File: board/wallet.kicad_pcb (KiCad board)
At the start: 4 copper layers, 48 x 85 mm, 108 parts, among them J1 TYPE-C-31-M-12, U1 BQ25185DLHR, U11 E73-2G4M08S1C, U12 ME6211C28M5G-N, U13 TPS60230RGTR, U14 TLV70313DBVR, U15 MAX17048G+T10, U2 TPS63802DLAR, U4 STM32U585VIT6Q, U5 SE050E2HQ1/Z01Z3Z, U6 TS3USB221ARSER, U7 SN74LVC1G02DBVR(UMW), U8 TPS22917DBVR, U9 TXU0202DCUR

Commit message: TP_NRST next to the MCU's NRST pin
The NRST test pad sat with the other programming pads on the west edge while
NRST is pin 14 on the MCU's east side, behind hand-routed copper: the autorouter
took 29.5 mm down the west edge for it. Now on the front at (33.6, 26.8), beside
NRST's 100 nF cap: 4.7 mm of copper, one via. Same move in the radio-gate
candidate. Unconnected 57 -> 56 on the main board.

Co-Authored-By: Claude Opus 5.5 <noreply@anthropic.com>
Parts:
- moved TP_NRST 29.6 mm to (33.6, 26.8)
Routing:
- net NRST: track 2.34 -> 4.73 mm, vias 0 -> 1
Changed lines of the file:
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@@
 	(footprint "TestPoint:TestPoint_Pad_D1.0mm"
 		(layer "F.Cu")
-		(at 4 25.56)
+		(at 33.6 26.8)
 		(descr "SMD pad as test Point, diameter 1.0mm")
 		(tags "test point SMD pad")
@@
 	)
 	(segment
+		(start 33.425 26.8)
+		(end 32.35 27.875)
+		(width 0.15)
+		(layer "F.Cu")
+		(net "NRST")
+	)
+	(segment
+		(start 33.6 26.8)
+		(end 33.425 26.8)
+		(width 0.15)
+		(layer "F.Cu")
+		(net "NRST")
+	)
+	(via
+		(at 32.35 27.875)
+		(size 0.45)
+		(drill 0.25)
+		(layers "F.Cu" "B.Cu")
+		(net "NRST")
+	)
+	(segment
 		(start 31.89 28.5)
 		(end 31.98 28.41)
 		(width 0.15)
+		(layer "B.Cu")
+		(net "NRST")
+	)
+	(segment
+		(start 32.35 27.875)
+		(end 32.35 28.04)
+		(width 0.15)
+		(layer "B.Cu")
+		(net "NRST")
+	)
+	(segment
+		(start 32.35 28.04)
+		(end 31.98 28.41)
+		(width 0.15)

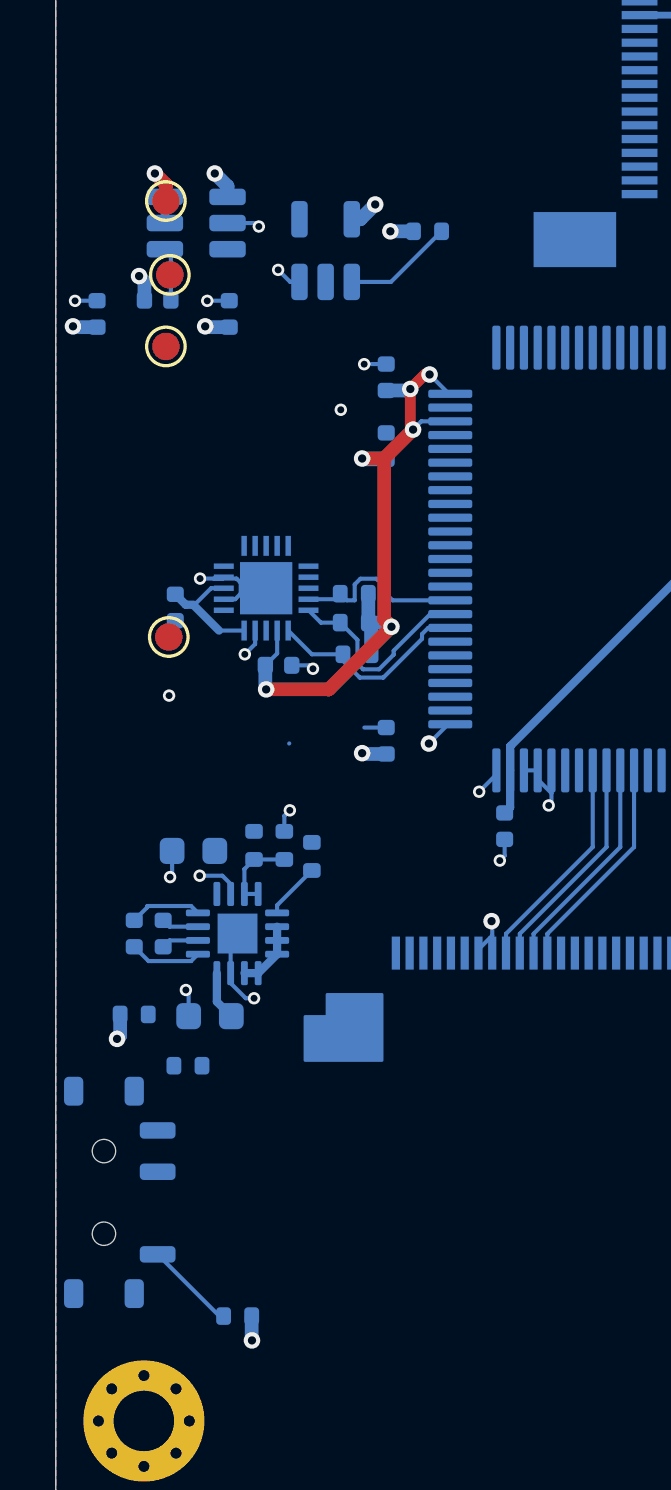
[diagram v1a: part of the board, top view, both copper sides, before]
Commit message: Radio gate beside the airgap switch (merged from the experiment)
The NOR and the load switch with their parts move from the north-west corner
to beside the airgap switch: AIRGAP and RADIO_3V3, which ran 30-40 mm down the
west side, are now a few millimetres. Gauge (full autoroute on a copy, same
settings): 10 % less copper to route (1260 vs 1395 mm), 5 fewer signal vias.
Only the radio gate's parts and my copper at them changed; the owner's copper
is untouched. Open: one 2.7 mm 3.3 V link (CT cap to the airgap pull-up) for a
hand trace, no via fits there. UV art rebuilt.

Co-Authored-By: Claude Opus 5.5 <noreply@anthropic.com>
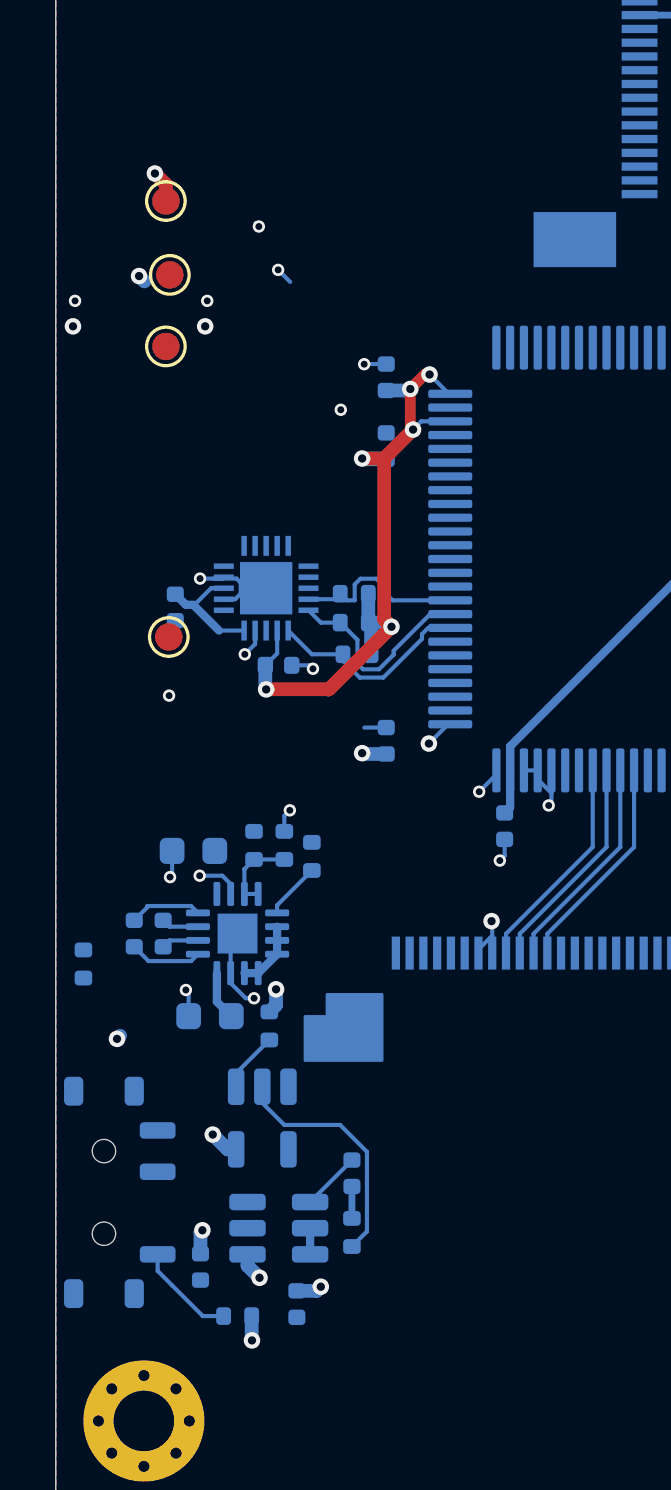
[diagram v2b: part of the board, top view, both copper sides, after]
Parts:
- moved C_RIN 36.7 mm to (8.75, 55.1), turned to -90 degrees
- moved U8 36.6 mm to (8.10, 52.3), turned to 0 degrees
- moved C_NOR 34.6 mm to (5.25, 53.7), turned to -90 degrees
- moved C_RCT 32.5 mm to (10.8, 50.3), turned to 90 degrees
- moved U7 31.6 mm to (7.50, 48.3), turned to -90 degrees
- moved R_ROFF 29.4 mm to (7.75, 45.0), turned to 90 degrees
- moved R_AIRPU 11.2 mm to (10.8, 52.5), turned to 90 degrees
- moved R_AIRS 5.30 mm to (1.00, 42.7), turned to 90 degrees
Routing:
- net AIRGAP: track 0.00 -> 8.79 mm
- net GND: track 81.9 -> 79.0 mm
- net RADIO_OFF: track 4.02 -> 2.20 mm
- net V3V3: track 112.7 -> 112.6 mm, vias 45 -> 47

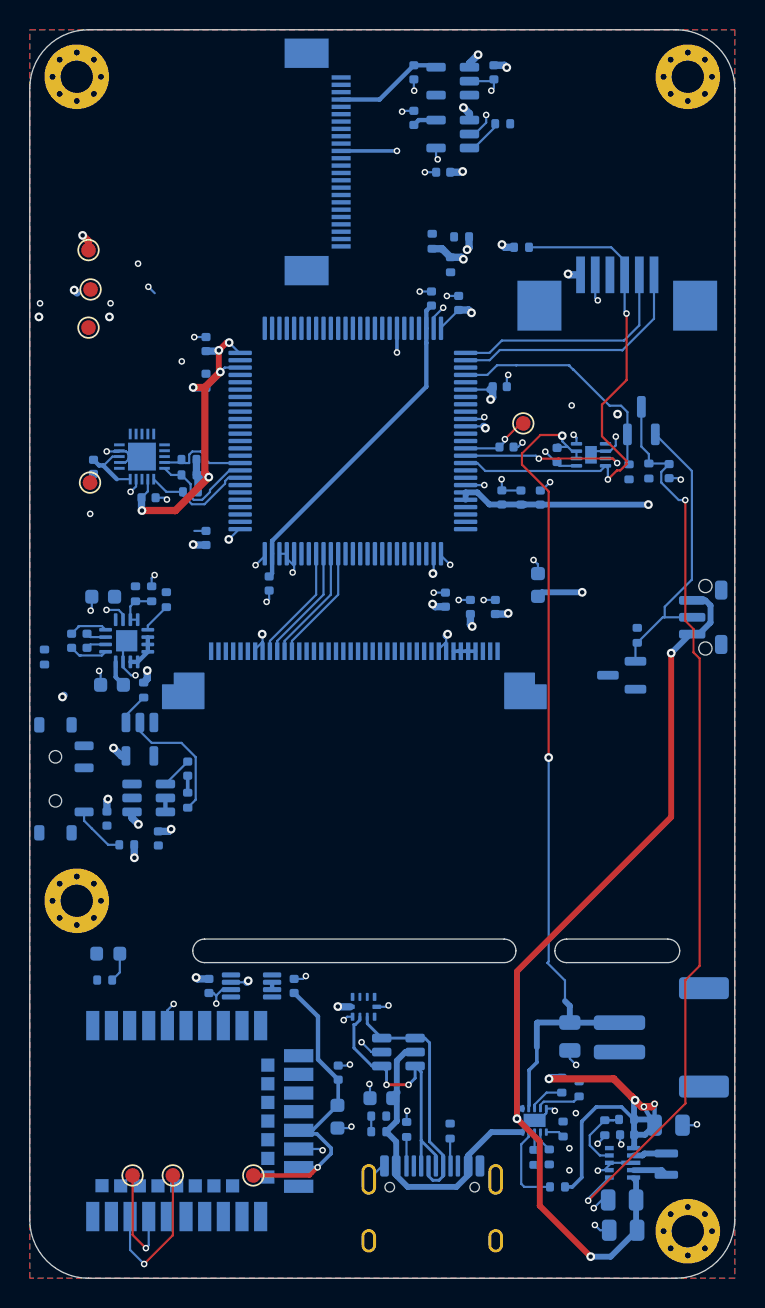
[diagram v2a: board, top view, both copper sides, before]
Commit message: Owner: north camera pins, radio UART, display control, button and 3.3 V cleanup
Hand-routed the camera bus's north-side pins (VSYNC, XCLK, D4, D6, D7, RST,
SDA, EN), the radio UART from the module to the TXU0202, TFT_TE/RST, BTN/BTN_N,
CTP_RST, I2C_SCL, AIRGAP, RADIO_3V3. Button transistor and resistor moved up by
the MCU, the AIRGAP_SENSE resistor inline by the MCU, the radio LED parts
shifted. 3.3 V cleanup: three stale plane vias (left where the radio gate's
parts used to be) and stubs removed; thin 0.15 mm 3.3 V links between a plane
via and its pad redone at 0.4 mm.

Co-Authored-By: Claude Opus 5.5 <noreply@anthropic.com>
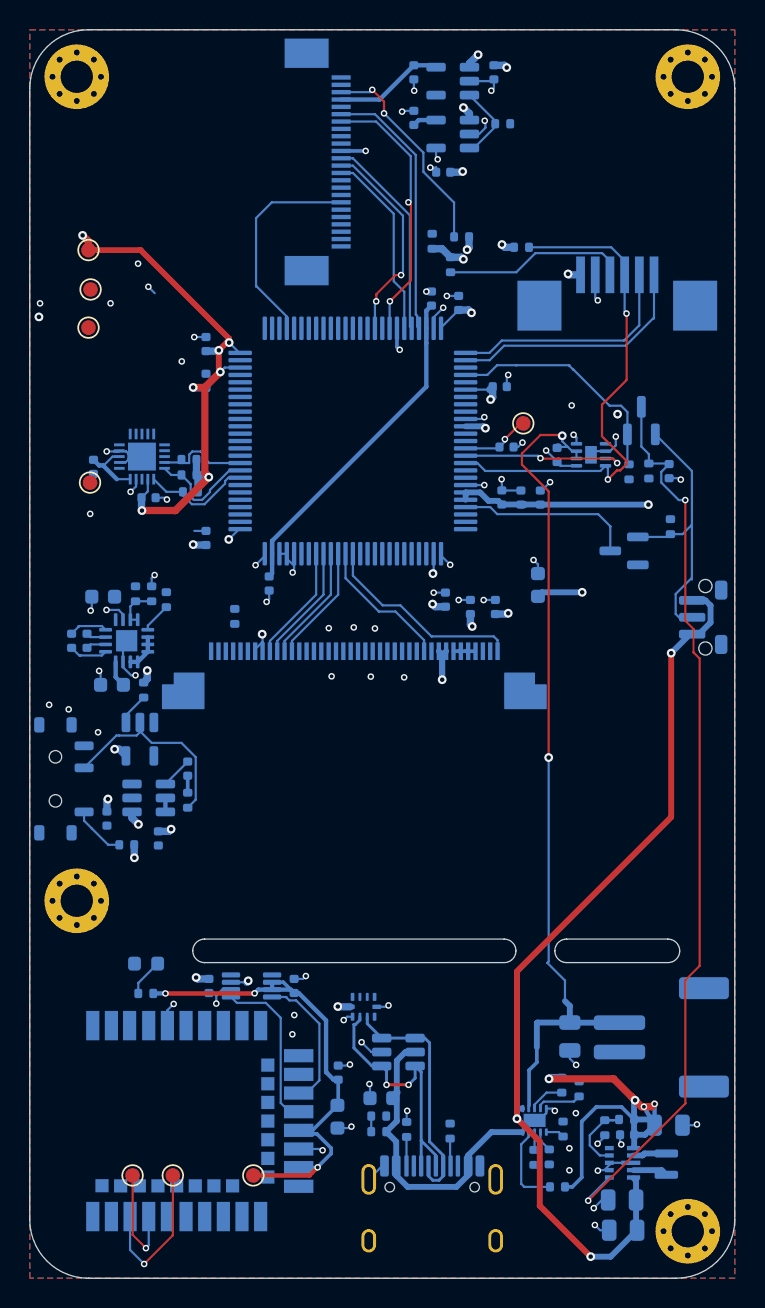
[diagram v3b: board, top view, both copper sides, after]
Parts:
- moved R_AIRS 13.2 mm to (14.0, 39.9)
- moved Q_BTN 8.47 mm to (40.5, 35.5)
- moved R_BTN 7.74 mm to (43.6, 33.8)
- moved R_RLED 2.94 mm to (7.90, 65.6), turned to 180 degrees
- moved D_RADIO 2.66 mm to (7.92, 63.6)
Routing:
- net CAM_VSYNC: track 0.00 -> 18.2 mm, vias 0 -> 2
- net CAM_RST: track 0.00 -> 18.1 mm
- net CAM_D4: track 0.00 -> 14.6 mm
- net CAM_SDA: track 0.00 -> 14.5 mm, vias 0 -> 2
- net CAM_XCLK: track 0.00 -> 14.3 mm, vias 0 -> 2
- net CAM_D7: track 0.00 -> 14.0 mm
- net TFT_TE: track 0.00 -> 13.9 mm
- net CAM_D6: track 0.00 -> 12.8 mm
- net I2C_SCL: track 11.5 -> 24.1 mm
- net BTN_N: track 0.00 -> 12.1 mm
- net RADIO_3V3: track 23.3 -> 35.3 mm, vias 1 -> 3
- net V3V3: track 112.6 -> 124.4 mm, vias 47 -> 44
- net RADIO_TX: track 0.00 -> 11.2 mm
- net RADIO_RX: track 0.00 -> 10.2 mm
- net TFT_RST: track 0.00 -> 9.51 mm
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
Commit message: Owner's cleanup rules as tools: stale copper out, power fanouts at full width
scripts/cleanCopper.py removes copper that touches none of its net's pads
(plane vias left where a part used to be, orphans; GND stitching is kept) and
sub-0.2 mm dangling crumbs, and refuses to write if KiCad's DRC gets worse.
scripts/widenFanouts.py widens each short pad-to-via link of a power net to
0.4 mm, capped at the pad's narrow side, undoing any widening DRC objects to.

Applied: two more stale V3V3 vias (old radio-gate spot, old front trunk) and
two crumbs gone; 17 thin 3.3 V links widened (MCU pins 0.15 -> 0.30 mm, the pin
width). Unconnected 40 -> 40, no new DRC findings.

Co-Authored-By: Claude Opus 5.5 <noreply@anthropic.com>
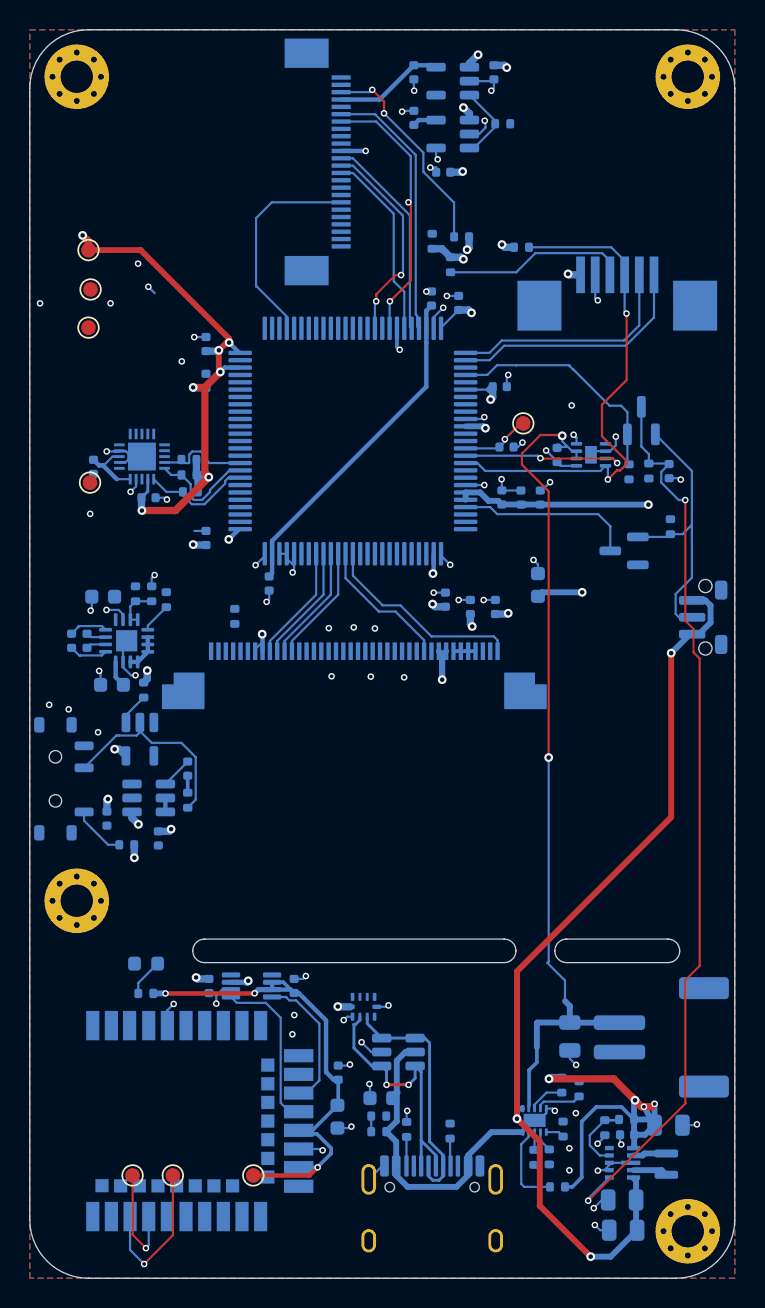
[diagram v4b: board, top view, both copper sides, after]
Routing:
- net V3V3: track 124.4 -> 124.3 mm, vias 44 -> 42
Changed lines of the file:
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@@
 	)
 	(via
-		(at 0.625 19.55)
-		(size 0.6)
-		(drill 0.3)
-		(layers "F.Cu" "B.Cu")
-		(net "V3V3")
-	)
-	(via
 		(at 29.525 5.3)
 		(size 0.6)
@@
 	)
 	(via
-		(at 40.02 26.17)
-		(size 0.6)
-		(drill 0.3)
-		(layers "F.Cu" "B.Cu")
-		(net "V3V3")
-	)
-	(via
 		(at 12.19 30.46)
 		(size 0.6)
@@
 		(start 14.25 34)
 		(end 13.55 34.7)
-		(width 0.15)
+		(width 0.3)
 		(layer "B.Cu")
 		(net "V3V3")
@@
 		(start 13.7 64.849999)
 		(end 14.775001 64.849999)
-		(width 0.15)
+		(width 0.35)
 		(layer "B.Cu")
 		(net "V3V3")
@@
 		(start 27.5 35.675)
 		(end 27.5 36.975)
-		(width 0.15)
+		(width 0.3)
 		(layer "B.Cu")
 		(net "V3V3")
@@
 		(start 15.85 42.309999)
 		(end 15.85 41.175)
-		(width 0.15)
+		(width 0.3)
 		(layer "B.Cu")
 		(net "V3V3")
@@
 		(start 8.04 31.43)
 		(end 7.61 31.86)
-		(width 0.15)
+		(width 0.2)
 		(layer "B.Cu")
 		(net "V3V3")
@@
 		(start 22.87 8.25)
 		(end 21.2 8.25)
-		(width 0.25)
+		(width 0.3)
 		(layer "B.Cu")
 		(net "V3V3")
@@
 		(start 14.325 22)
 		(end 14.275 22)
-		(width 0.15)
+		(width 0.3)
 		(layer "B.Cu")
 		(net "V3V3")
@@
 		(start 42.54 74.58)
 		(end 42.54 73.13)
-		(width 0.3)
+		(width 0.4)
 		(layer "B.Cu")
 		(net "V3V3")
@@
 	)
 	(segment
-		(start 39.98 26.21)
-		(end 40.02 26.17)
-		(width 0.15)
-		(layer "B.Cu")
-		(net "V3V3")
-	)
-	(segment
 		(start 34.751421 32.321421)
 		(end 34.76 32.33)
@@
 		(start 14.275 22)
 		(end 13.575 21.3)
-		(width 0.15)
+		(width 0.3)
 		(layer "B.Cu")
 		(net "V3V3")
@@
 		(start 14.325 34)
 		(end 14.25 34)
-		(width 0.15)
-		(layer "B.Cu")
-		(net "V3V3")
-	)
-	(segment
-		(start 0.655 19.58)
-		(end 0.625 19.55)
-		(width 0.5)
+		(width 0.3)
 		(layer "B.Cu")
 		(net "V3V3")
@@
 		(start 14.325 23)
 		(end 13.275 23)
-		(width 0.15)
+		(width 0.3)
 		(layer "B.Cu")
 		(net "V3V3")
@@
 		(start 8.04 30.598)
 		(end 8.04 31.43)
-		(width 0.15)
+		(width 0.2)
 		(layer "B.Cu")
 		(net "V3V3")
@@
 		(start 13.275 23)
 		(end 12.975 23.3)
-		(width 0.15)
+		(width 0.3)
 		(layer "B.Cu")
 		(net "V3V3")
@@
 		(start 42.54 74.58)
 		(end 41.815 73.324264)
-		(width 0.3)
+		(width 0.4)
 		(layer "B.Cu")
 		(net "V3V3")
@@
 		(start 15.560001 65.349999)
 		(end 15.31 65.6)
-		(width 0.3)
+		(width 0.35)
 		(layer "B.Cu")
 		(net "RADIO_3V3")
@@
 		(start 16.5 65.349999)
 		(end 15.560001 65.349999)
-		(width 0.3)
+		(width 0.35)
 		(layer "B.Cu")
 		(net "RADIO_3V3")
@@
 		(start 9.24 65.61)
 		(end 8.41 65.61)
-		(width 0.3)
+		(width 0.4)
 		(layer "B.Cu")
 		(net "RADIO_3V3")
@@
 	)
 	(segment
-		(start 45.08 37.31)
-		(end 45.08 37.435514)
-		(width 0.15)
-		(layer "B.Cu")
-		(net "BTN")
-	)
-	(segment
 		(start 43.62 34.34)
 		(end 44.44 34.34)
@@
 		(width 0.15)
 		(layer "B.Cu")
-		(net "CTP_RST")
-	)
-	(segment
-		(start 42.5 19.67)
-		(end 42.5 19.59)
-		(width 0.15)
-		(layer "B.Cu")

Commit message: 3.3 V power done, block wiring autorouted, stale copper gone
Power: every V3V3 and RADIO_3V3 pad reaches the In1 plane on a fanout as
thick as its pad allows (0.4 mm, capped at the pad's narrow side); SYS,
CAM_DVDD and the backlight supply are routed. The C_RCT/R_AIRPU 3.3 V pocket
had no room for a via and no way out (the AIRGAP track closed it): R_AIRPU
turned horizontal outside it and C_RCT joined to C_RIN pin to pin
(partialRoute.py --link, new).

Signals: the autorouted nets were accepted one by one (length near the
shortest tree, no added detour, hairpin or via): the camera west group,
CAM_D5, CAM_EN, the charger control/status lines, RADIO_OFF/EN, TFT_BL,
AIRGAP_SENSE, I2C_SCL, SWCLK/SWDIO, VBUS_SENSE. Left for the hand, ripped:
the USB pair (unpaired, hairpin), RADIO_TXD/RXD (twice the possible length)
and AIRGAP.

Clean: no pad-less copper, no crumbs (cleanCopper finds nothing); the B.Cu
GND pour piece under J_CAM/MCU north is stitched with two vias.

Unconnected 40 -> 6 (those three pairs); 0 copper DRC violations; nets,
MCU AF, sync, pin tables, FPC and parts gates pass. UV art rebuilt.

Co-Authored-By: Claude Opus 5.5 <noreply@anthropic.com>
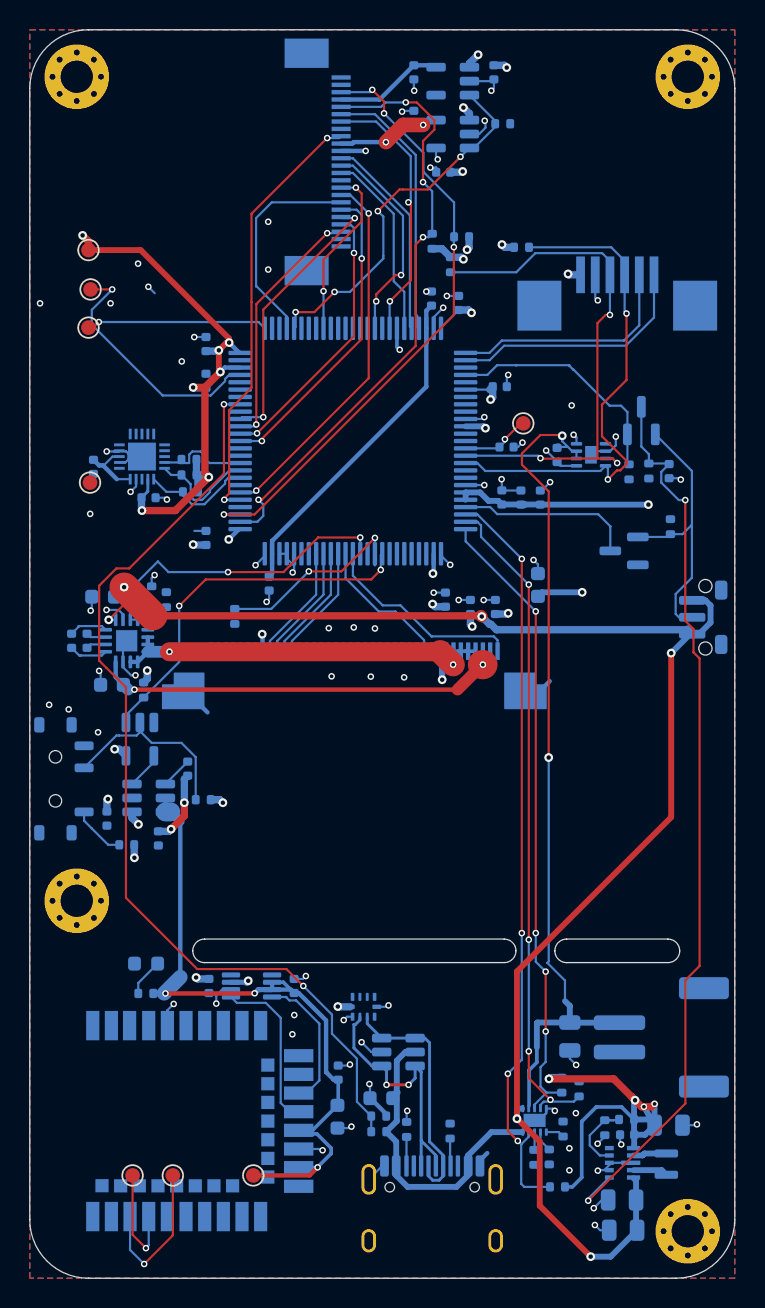
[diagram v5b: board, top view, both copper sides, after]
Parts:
- moved R_AIRPU 1.06 mm to (11.8, 52.4), turned to 0 degrees
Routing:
- net VBUS_SENSE: track 1.06 -> 65.9 mm, vias 0 -> 2
- net CHG_STAT1: track 5.78 -> 51.5 mm, vias 0 -> 4
- net SYS: track 62.1 -> 105.8 mm, vias 3 -> 6
- net CHG_CE: track 3.12 -> 45.5 mm, vias 0 -> 4
- net CAM_SCL: track 0.00 -> 41.6 mm, vias 0 -> 4
- net CHG_STAT2: track 2.71 -> 43.6 mm, vias 0 -> 4
- net CAM_HREF: track 0.00 -> 29.6 mm, vias 0 -> 2
- net CAM_SDA: track 14.5 -> 42.2 mm, vias 2 -> 4
- net BL_A: track 1.78 -> 28.0 mm, vias 0 -> 2
- net CAM_PCLK: track 0.00 -> 25.6 mm, vias 0 -> 2
- net RADIO_OFF: track 2.20 -> 25.3 mm, vias 0 -> 2
- net BL_K: track 4.28 -> 25.8 mm, vias 0 -> 2
- net CAM_D0: track 0.00 -> 21.2 mm, vias 0 -> 2
- net CAM_EN: track 5.23 -> 25.3 mm, vias 0 -> 4
- net CAM_D1: track 0.00 -> 18.8 mm, vias 0 -> 2
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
